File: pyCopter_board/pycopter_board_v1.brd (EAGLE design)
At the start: 78.7 x 77.5 mm, 36 parts, among them Q1 32.768kHz, U1 BNO055, U3 BMP180

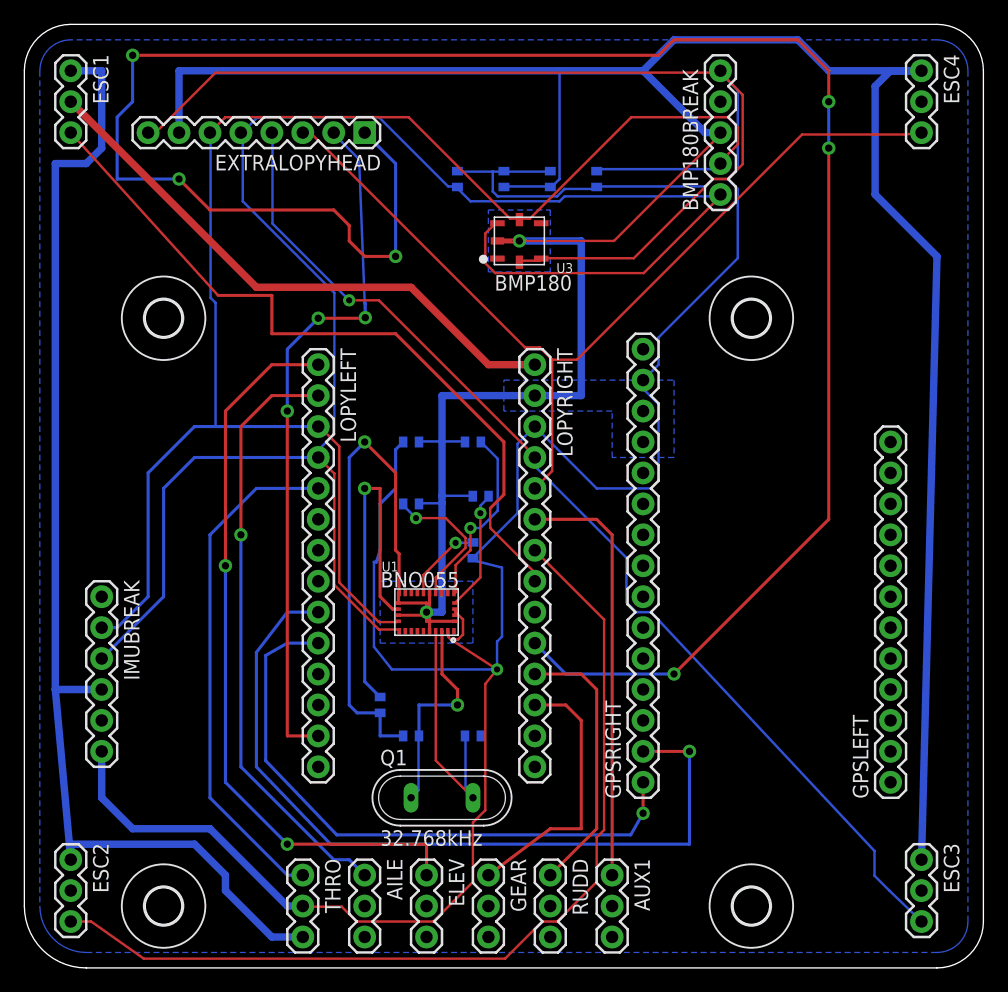
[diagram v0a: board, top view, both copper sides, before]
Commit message: made traces wider and added a top ground plane at the suggestion of charlie. also added text labels around the header pins.
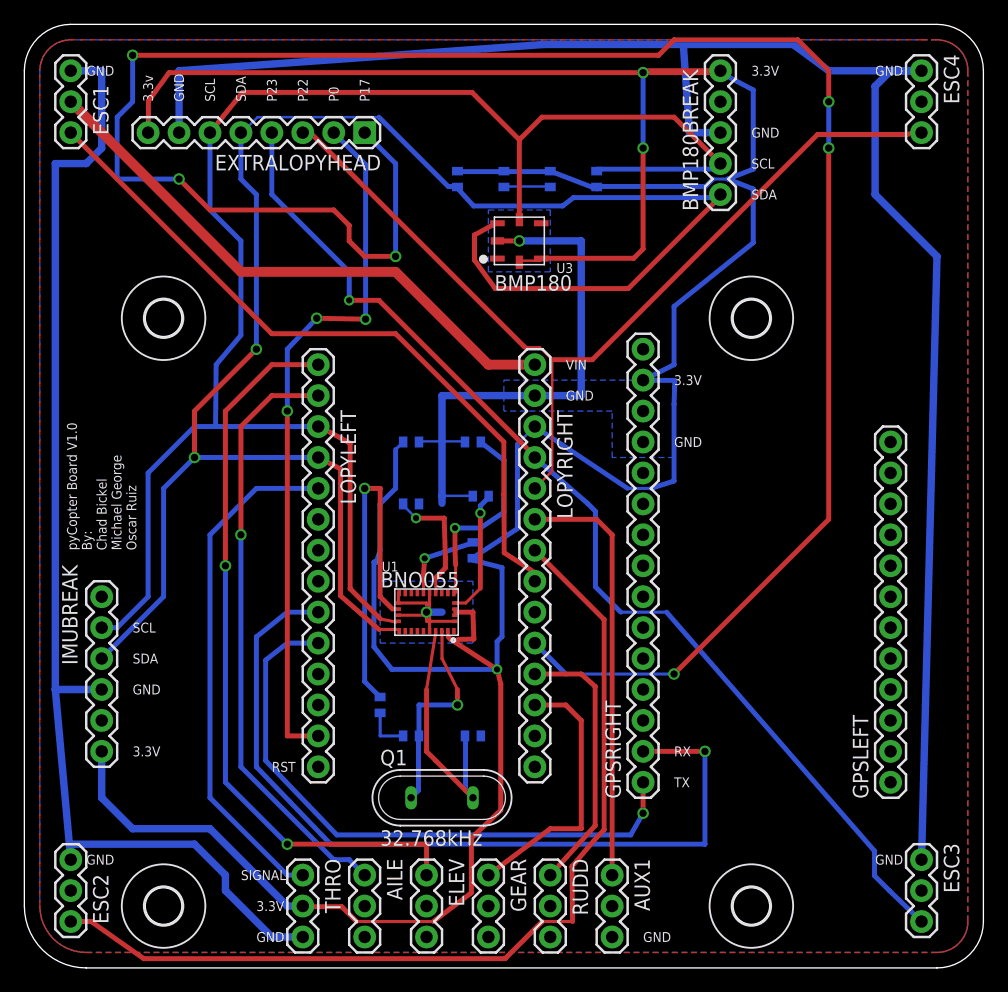
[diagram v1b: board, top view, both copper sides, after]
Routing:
- net GND: track 394.0 -> 315.0 mm, vias 3 -> 2
- net 3.3V: track 280.2 -> 287.5 mm, vias 1 -> 3
- net GPS_RX: track 65.8 -> 68.7 mm
- net P19: track 61.7 -> 58.9 mm
- net SDA: track 147.5 -> 150.2 mm, vias 0 -> 2
- net N$3: track 15.0 -> 16.5 mm
- net P23: track 88.7 -> 90.2 mm
- net N$1: track 11.9 -> 10.4 mm
- net SCL: track 139.9 -> 141.4 mm
- net P0: track 59.2 -> 58.5 mm
- net P20: track 76.6 -> 77.3 mm
- net N$4: track 9.92 -> 10.5 mm
- added copper zone on layer 1, net GND
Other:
- board text added: "3.3V"
- board text added: "3.3v"
- board text added: "GND"
- board text added: "P0"
- board text added: "P17"
- board text added: "P22"
- board text added: "P23"
- board text added: "RST"
- board text added: "RX"
- board text added: "SCL"
- board text added: "SDA"
- board text added: "SIGNAL"
- board text added: "TX"
- board text added: "VIN"
- board text added: "pyCopter Board V1.0 By: Chad Bickel Michael George Oscar Ruiz"

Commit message: added some more updates based upon charlie's suggestions.
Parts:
- Q1: device special:QS -> crystal:TC38H
- R5, R6: value 10K -> 2.2k
- moved Q1 7.62 mm to (34.3, 21.6), turned to 180 degrees
- moved C4 6.27 mm to (37.7, 21.0), flipped to the top, turned to 90 degrees
- moved C5 6.02 mm to (31.1, 21.0), flipped to the top, turned to 90 degrees
- moved R3 1.27 mm to (27.9, 21.6)
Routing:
- net XOUT: track 20.7 -> 8.29 mm
- net XIN: track 17.4 -> 8.76 mm, vias 1 -> 0
- net GND: track 315.0 -> 313.1 mm, vias 2 -> 6
- net N$2: track 29.7 -> 29.2 mm
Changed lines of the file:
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@@
 <attribute name="VALUE" x="31.6865" y="38.862" size="0.4064" layer="26" font="vector" ratio="15" rot="MR0"/>
 </element>
-<element name="C4" library="SparkFun-Passives" package="0402-CAP" value="22pF" x="31.75" y="19.05" smashed="yes" rot="MR180">
-<attribute name="NAME" x="30.861" y="18.3515" size="0.4064" layer="26" font="vector" ratio="15" rot="MR180"/>
-<attribute name="VALUE" x="30.6705" y="20.193" size="0.4064" layer="26" font="vector" ratio="15" rot="MR180"/>
-</element>
-<element name="C5" library="SparkFun-Passives" package="0402-CAP" value="22pF" x="36.83" y="19.05" smashed="yes" rot="MR0">
-<attribute name="NAME" x="37.719" y="19.7485" size="0.4064" layer="26" font="vector" ratio="15" rot="MR0"/>
-<attribute name="VALUE" x="37.9095" y="17.907" size="0.4064" layer="26" font="vector" ratio="15" rot="MR0"/>
+<element name="C4" library="SparkFun-Passives" package="0402-CAP" value="22pF" x="37.719" y="20.955" smashed="yes" rot="R90">
+<attribute name="NAME" x="37.0205" y="20.066" size="0.4064" layer="25" font="vector" ratio="15" rot="R90"/>
+<attribute name="VALUE" x="38.862" y="19.8755" size="0.4064" layer="25" font="vector" ratio="15" rot="R90"/>
+</element>
+<element name="C5" library="SparkFun-Passives" package="0402-CAP" value="22pF" x="31.115" y="20.955" smashed="yes" rot="R90">
+<attribute name="NAME" x="31.115" y="19.05" size="0.4064" layer="25" font="vector" ratio="15"/>
+<attribute name="VALUE" x="31.0515" y="18.542" size="0.4064" layer="25" font="vector" ratio="15"/>
 </element>
 <element name="C6" library="SparkFun-Passives" package="0402-CAP" value="10uF" x="39.37" y="64.77" smashed="yes" rot="MR90">
@@
 <attribute name="VALUE" x="3.175" y="31.75" size="1.27" layer="27" rot="R270"/>
 </element>
-<element name="Q1" library="special" package="QS" value="32.768kHz" x="34.29" y="13.97" smashed="yes">
-<attribute name="VALUE" x="29.21" y="10.033" size="1.27" layer="25" font="vector" ratio="15"/>
-<attribute name="NAME" x="29.21" y="16.637" size="1.27" layer="25" font="vector" ratio="15"/>
+<element name="Q1" library="crystal" package="TC38H" value="32.768kHz" x="34.29" y="21.59" smashed="yes" rot="R180">
+<attribute name="VALUE" x="29.083" y="21.59" size="1.27" layer="25" font="vector" ratio="15" rot="R270"/>
+<attribute name="NAME" x="39.37" y="18.923" size="1.27" layer="25" font="vector" ratio="15" rot="R180"/>
+<attribute name="MPN" value="" x="34.29" y="21.59" size="1.778" layer="27" rot="R180" display="off"/>
+<attribute name="OC_NEWARK" value="unknown" x="34.29" y="21.59" size="1.778" layer="27" rot="R180" display="off"/>
+<attribute name="OC_FARNELL" value="unknown" x="34.29" y="21.59" size="1.778" layer="27" rot="R180" display="off"/>
+<attribute name="MF" value="" x="34.29" y="21.59" size="1.778" layer="27" rot="R180" display="off"/>
 </element>
 <element name="R1" library="SparkFun-Passives" package="0402-RES" value="10K" x="36.83" y="43.18" smashed="yes" rot="MR180">
@@
 <attribute name="VALUE" x="36.3855" y="39.878" size="0.4064" layer="26" font="vector" ratio="15" rot="MR180"/>
 </element>
-<element name="R3" library="SparkFun-Passives" package="0402-RES" value="10K" x="29.21" y="21.59" smashed="yes" rot="MR90">
-<attribute name="NAME" x="29.9085" y="20.701" size="0.4064" layer="26" font="vector" ratio="15" rot="MR90"/>
-<attribute name="VALUE" x="28.067" y="20.5105" size="0.4064" layer="26" font="vector" ratio="15" rot="MR90"/>
+<element name="R3" library="SparkFun-Passives" package="0402-RES" value="10K" x="27.94" y="21.59" smashed="yes" rot="MR90">
+<attribute name="NAME" x="28.6385" y="20.701" size="0.4064" layer="26" font="vector" ratio="15" rot="MR90"/>
+<attribute name="VALUE" x="26.797" y="20.5105" size="0.4064" layer="26" font="vector" ratio="15" rot="MR90"/>
 </element>
 <element name="R4" library="SparkFun-Passives" package="0402-RES" value="10K" x="36.83" y="34.29" smashed="yes" rot="MR90">
@@
 <attribute name="VALUE" x="35.687" y="33.2105" size="0.4064" layer="26" font="vector" ratio="15" rot="MR90"/>
 </element>
-<element name="R5" library="SparkFun-Passives" package="0402-RES" value="10K" x="35.56" y="64.77" smashed="yes" rot="MR90">
+<element name="R5" library="SparkFun-Passives" package="0402-RES" value="2.2k" x="35.56" y="64.77" smashed="yes" rot="MR90">
 <attribute name="NAME" x="36.2585" y="63.881" size="0.4064" layer="26" font="vector" ratio="15" rot="MR90"/>
 <attribute name="VALUE" x="34.417" y="63.6905" size="0.4064" layer="26" font="vector" ratio="15" rot="MR90"/>
 </element>
-<element name="R6" library="SparkFun-Passives" package="0402-RES" value="10K" x="46.99" y="64.77" smashed="yes" rot="MR270">
+<element name="R6" library="SparkFun-Passives" package="0402-RES" value="2.2k" x="46.99" y="64.77" smashed="yes" rot="MR270">
 <attribute name="NAME" x="46.2915" y="65.659" size="0.4064" layer="26" font="vector" ratio="15" rot="MR270"/>
 <attribute name="VALUE" x="48.133" y="65.8495" size="0.4064" layer="26" font="vector" ratio="15" rot="MR270"/>
@@
 <wire x1="57.15" y1="68.4276" x2="57.15" y2="68.58" width="0.2032" layer="1"/>
 <wire x1="30.734" y1="30.8356" x2="30.77" y2="30.7725" width="0.2032" layer="1"/>
-<wire x1="29.21" y1="20.94" x2="29.21" y2="19.05" width="0.254" layer="16"/>
-<wire x1="29.21" y1="19.05" x2="31.1" y2="19.05" width="0.254" layer="16"/>
+<wire x1="27.94" y1="20.94" x2="27.94" y2="19.05" width="0.254" layer="16"/>
 <polygon width="0.254" layer="16" isolate="0.3048" rank="6">
 <vertex x="5.08" y="1.27"/>
@@
 <vertex x="3.81" y="76.2"/>
 </polygon>
-<wire x1="39.37" y1="64.12" x2="38.84" y2="59.69" width="0" layer="19" extent="1-16"/>
+<via x="37.592" y="64.008" extent="1-16" drill="0.6" shape="square"/>
+<via x="34.29" y="62.23" extent="1-16" drill="0.6" shape="square"/>
+<via x="35.179" y="67.945" extent="1-16" drill="0.6" shape="square"/>
+<via x="45.339" y="67.818" extent="1-16" drill="0.6" shape="square"/>
 </signal>
 <signal name="3.3V">
@@
 <contactref element="Q1" pad="2"/>
 <contactref element="C5" pad="2"/>
-<wire x1="36.83" y1="13.97" x2="33.782" y2="17.018" width="0.4064" layer="1"/>
 <wire x1="33.782" y1="27.5844" x2="33.77" y2="27.6475" width="0.2032" layer="1"/>
-<wire x1="36.2204" y1="14.5796" x2="36.2204" y2="19.05" width="0.4064" layer="16"/>
-<wire x1="36.83" y1="13.97" x2="36.2204" y2="14.5796" width="0.4064" layer="16"/>
-<wire x1="36.2204" y1="19.05" x2="36.18" y2="19.05" width="0.2032" layer="16"/>
-<wire x1="33.782" y1="27.5844" x2="33.02" y2="22.86" width="0.254" layer="1"/>
-<wire x1="33.02" y1="22.86" x2="33.02" y2="17.78" width="0.4064" layer="1"/>
-<wire x1="33.02" y1="17.78" x2="33.782" y2="17.018" width="0.4064" layer="1"/>
+<wire x1="33.782" y1="27.5844" x2="33.782" y2="22.352" width="0.254" layer="1"/>
+<wire x1="33.782" y1="22.352" x2="33.02" y2="21.59" width="0.4064" layer="1"/>
+<wire x1="31.115" y1="21.605" x2="33.005" y2="21.605" width="0.4064" layer="1"/>
+<wire x1="33.005" y1="21.605" x2="33.02" y2="21.59" width="0.4064" layer="1"/>
 </signal>
 <signal name="XIN">
@@
 <contactref element="Q1" pad="1"/>
 <contactref element="C4" pad="2"/>
-<wire x1="32.3596" y1="14.5796" x2="32.3596" y2="19.05" width="0.4064" layer="16"/>
-<wire x1="31.75" y1="13.97" x2="32.3596" y2="14.5796" width="0.4064" layer="16"/>
-<wire x1="32.3596" y1="19.05" x2="32.4" y2="19.05" width="0.2032" layer="16"/>
-<wire x1="32.4" y1="19.05" x2="32.4" y2="21.59" width="0.4064" layer="16"/>
-<wire x1="32.4" y1="21.59" x2="35.56" y2="21.59" width="0.4064" layer="16"/>
-<via x="35.56" y="21.59" extent="1-16" drill="0.6" shape="square"/>
-<wire x1="35.56" y1="21.59" x2="35.56" y2="22.86" width="0.4064" layer="1"/>
-<wire x1="35.56" y1="22.86" x2="34.29" y2="25.4" width="0.254" layer="1"/>
-<wire x1="34.29" y1="25.4" x2="34.29" y2="27.6275" width="0.254" layer="1"/>
 <wire x1="34.29" y1="27.6275" x2="34.27" y2="27.6475" width="0.254" layer="1"/>
+<wire x1="34.29" y1="27.6275" x2="34.29" y2="22.86" width="0.254" layer="1"/>
+<wire x1="34.29" y1="22.86" x2="34.544" y2="22.606" width="0.254" layer="1"/>
+<wire x1="34.544" y1="22.606" x2="35.56" y2="21.59" width="0.4064" layer="1"/>
+<wire x1="35.56" y1="21.59" x2="37.704" y2="21.59" width="0.4064" layer="1"/>
+<wire x1="37.704" y1="21.59" x2="37.719" y2="21.605" width="0.4064" layer="1"/>
 </signal>
 <signal name="N$2">
 <contactref element="U1" pad="17"/>
 <contactref element="R3" pad="2"/>
-<wire x1="29.21" y1="22.24" x2="27.94" y2="23.51" width="0.4064" layer="16"/>
-<wire x1="27.94" y1="23.51" x2="27.94" y2="39.37" width="0.4064" layer="16"/>
+<wire x1="27.94" y1="22.24" x2="27.94" y2="39.37" width="0.4064" layer="16"/>
 <via x="27.94" y="39.37" extent="1-16" drill="0.6" shape="square"/>
 <wire x1="27.94" y1="39.37" x2="29.21" y2="39.37" width="0.4064" layer="1"/>
